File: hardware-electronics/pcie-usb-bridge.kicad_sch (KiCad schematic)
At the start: 0 parts

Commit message: SCH organise schematic #7
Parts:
- added U3: PI7C9X440SLBFDE, M2SmartHomeFootprints:PI7C9X440SLBFDE, symbol M2SmartHomeSymbols:PI7C9X440SLBFDE
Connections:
- new net: U3.100 (VDDC), U3.109 (VDDC), U3.111 (VDDC), U3.22 (VDDC), U3.35 (VDDC), U3.81 (VDDC)
- new net: U3.101 (VSS), U3.106 (VSS), U3.110 (VSS), U3.118 (VSS), U3.120 (VSS), U3.125 (VSS), U3.127 (VSS), U3.129 (VSS), U3.23 (VSS), U3.34 (VSS), U3.36 (VSS), U3.39 (VSS), U3.45 (VSS), U3.50 (VSS), U3.53 (VSS), U3.61 (VSS), U3.68 (VSS), U3.82 (VSS), U3.86 (VSS), U3.89 (VSS), U3.9 (VSS), U3.94 (VSS), U3.96 (VSS)
- new net: U3.105 (VDDR), U3.112 (VDDR), U3.33 (VDDR), U3.67 (VDDR), U3.8 (VDDR)
- new net: U3.115 (VDDA), U3.121 (VDDA), U3.122 (VDDA), U3.128 (VDDA), U3.83 (VDDA), U3.90 (VDDA), U3.91 (VDDA), U3.97 (VDDA)
- new net: U3.40 (AVDD), U3.46 (AVDD), U3.49 (AVDD), U3.60 (AVDD)

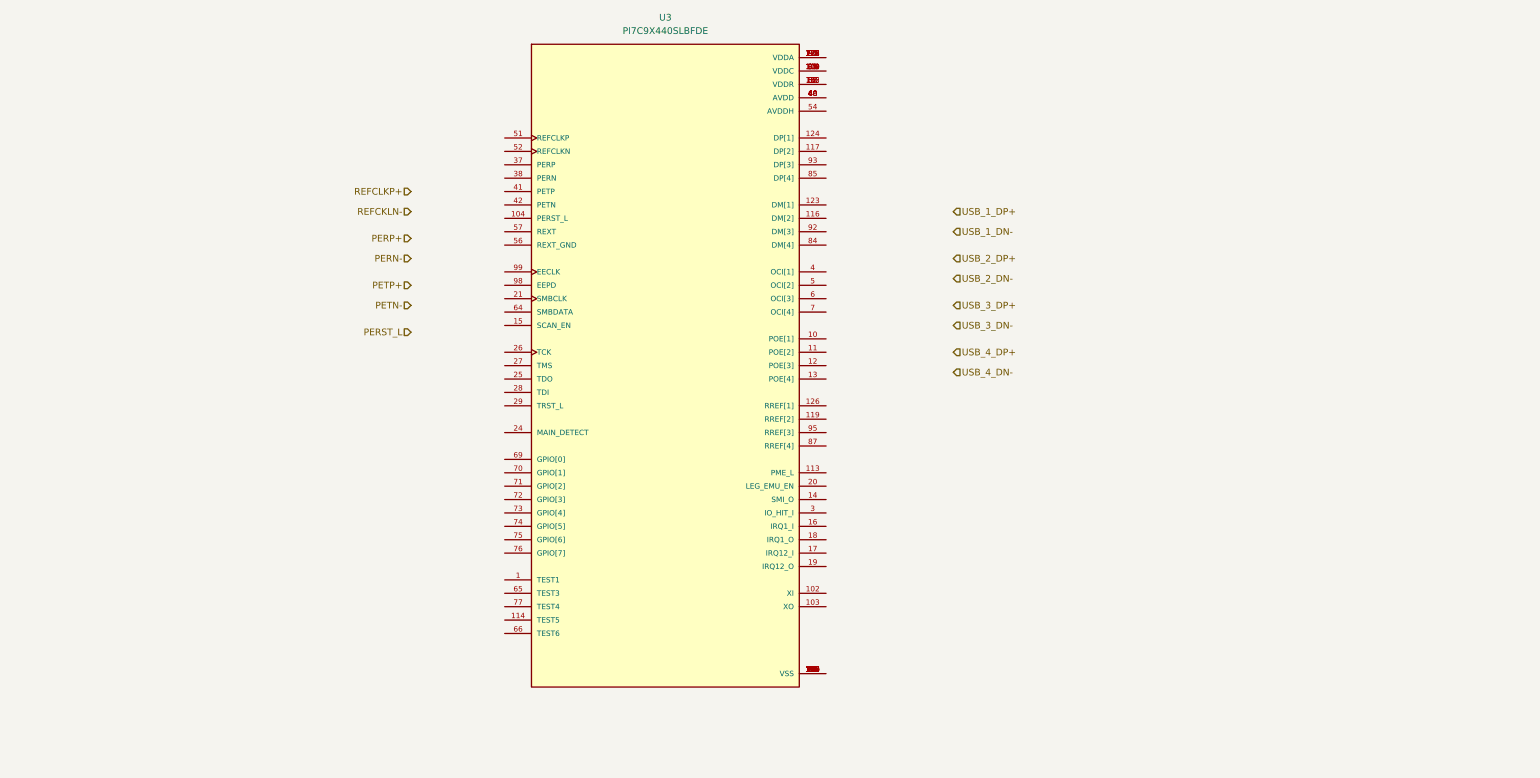
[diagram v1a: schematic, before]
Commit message: WIP SCH EMMC section
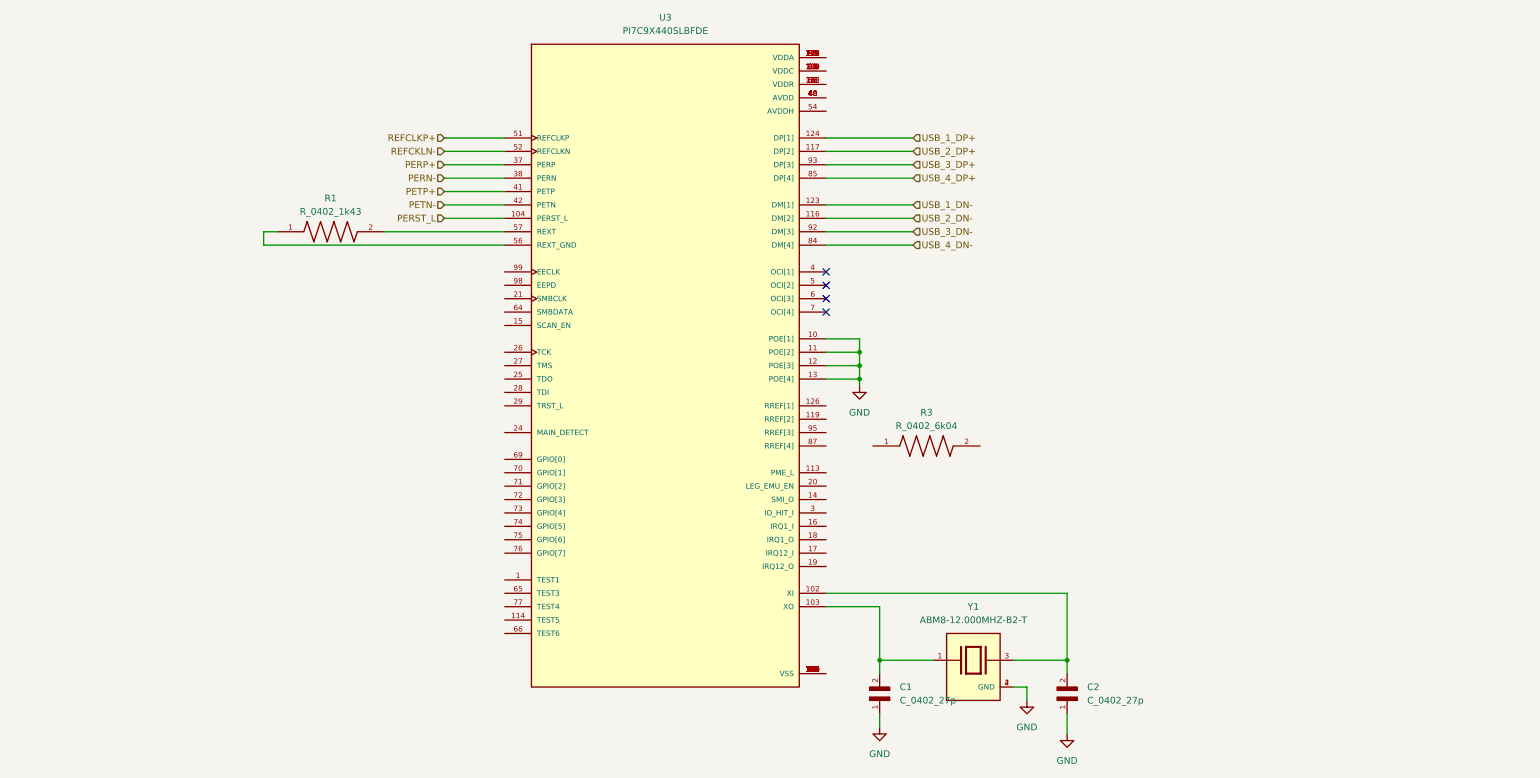
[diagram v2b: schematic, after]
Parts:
- added C1, C2: C_0402_27p, M2SmartHomeFootprints:CAPC1005X56N, symbol M2SmartHomeSymbols:04025A270FAT2A
- added R1: R_0402_1k43, M2SmartHomeFootprints:RESC1005X40N, symbol M2SmartHomeSymbols:RC0402FR-071K43L
- added R3: R_0402_6k04, M2SmartHomeFootprints:RES_ERJ2RKF6041X, symbol M2SmartHomeSymbols:ERJ2RKF6041X
- added Y1: ABM8-12.000MHZ-B2-T, M2SmartHomeFootprints:XTAL_ABM8-12.000MHZ-B2-T, symbol M2SmartHomeSymbols:ABM8-12.000MHZ-B2-T
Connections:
- net PERN-: now also U3.38 (PERN)
- net PERP+: now also U3.37 (PERP)
- net PERST_L: now also U3.104 (PERST_L)
- net PETN-: now also U3.42 (PETN)
- net PETP+: now also U3.41 (PETP)
- net REFCKLN-: now also U3.52 (REFCLKN)
- net REFCLKP+: now also U3.51 (REFCLKP)
- net USB_1_DN-: now also U3.123 (DM[1])
- net USB_1_DP+: now also U3.124 (DP[1])
- net USB_2_DN-: now also U3.116 (DM[2])
- net USB_2_DP+: now also U3.117 (DP[2])
- net USB_3_DN-: now also U3.92 (DM[3])
- net USB_3_DP+: now also U3.93 (DP[3])
- net USB_4_DN-: now also U3.84 (DM[4])
- net USB_4_DP+: now also U3.85 (DP[4])
- net GND: now reaches U3.10 (POE[1])
- net GND: now also U3.11 (POE[2]), U3.12 (POE[3]), U3.13 (POE[4]), C1.1, C2.1, Y1.2 (GND), Y1.4 (GND)
- net at U3.102 (XI): now also C2.2, Y1.3
- net at U3.103 (XO): now also C1.2, Y1.1
- net at U3.56 (REXT_GND): now also R1.1
- net at U3.57 (REXT): now also R1.2
- no-connect marks 0 -> 4

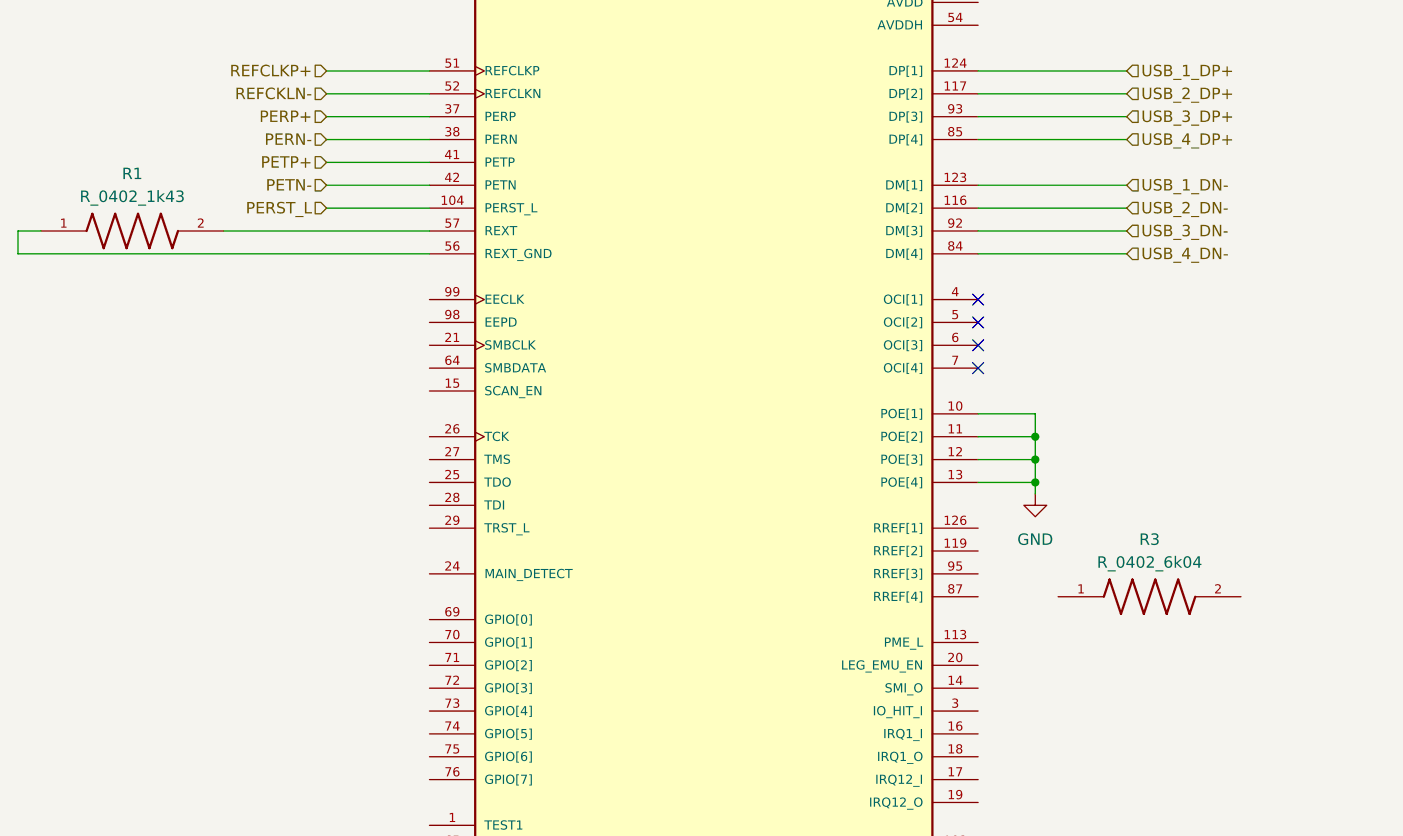
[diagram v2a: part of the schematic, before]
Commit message: [#8] SCH PCIe to USB replaced resistors
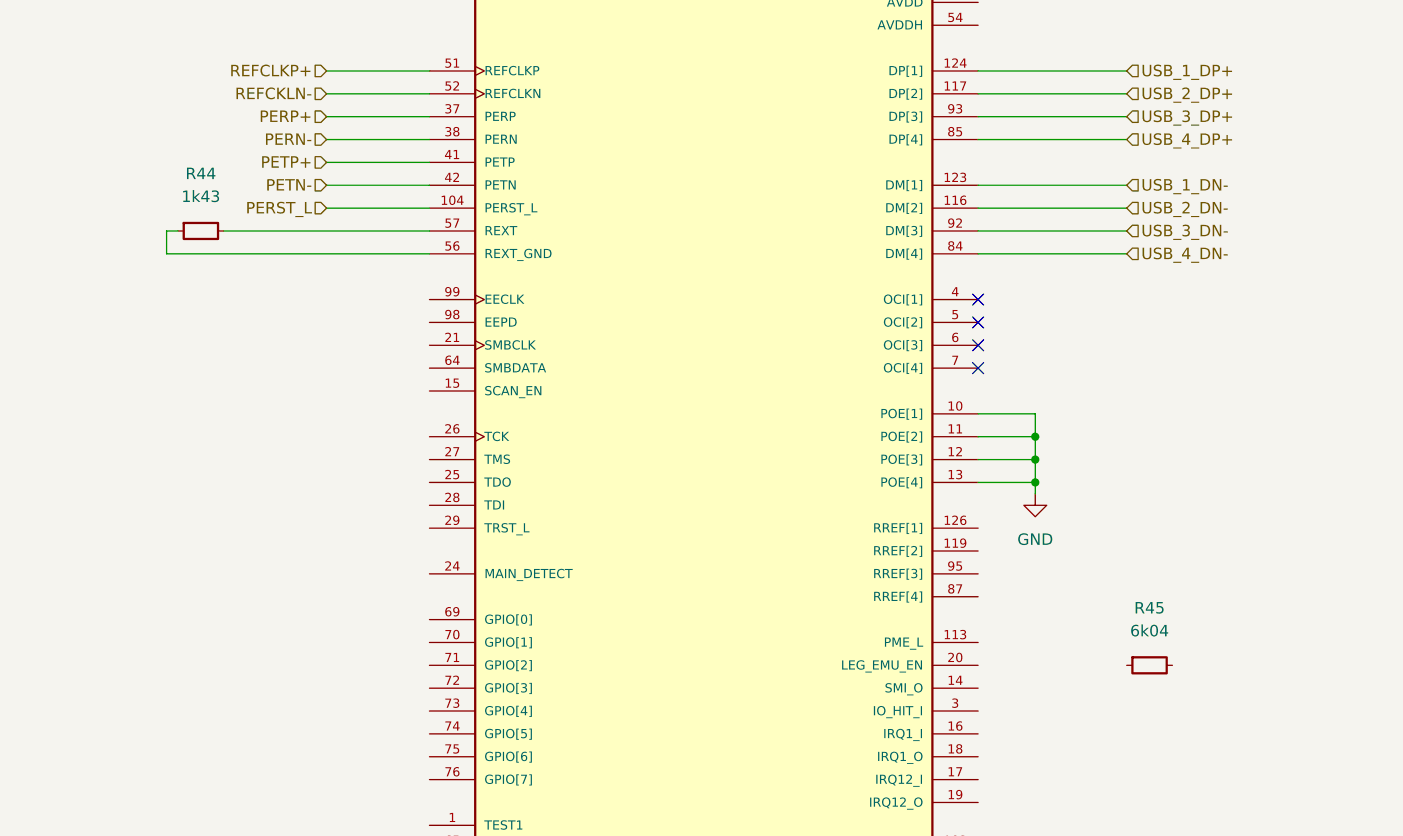
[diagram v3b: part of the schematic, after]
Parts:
- removed R1: R_0402_1k43, M2SmartHomeFootprints:RESC1005X40N, symbol M2SmartHomeSymbols:RC0402FR-071K43L
- removed R3: R_0402_6k04, M2SmartHomeFootprints:RES_ERJ2RKF6041X, symbol M2SmartHomeSymbols:ERJ2RKF6041X
- added R44: R_1k43_0402, M2SmartHomeFootprints:R_0402, symbol M2SmartHomeSymbols:R_1k43_0402
- added R45: R_6k04_0402, M2SmartHomeFootprints:R_0402, symbol M2SmartHomeSymbols:R_6k04_0402
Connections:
- net at U3.56 (REXT_GND): now also R44.1
- net at U3.57 (REXT): now also R44.2

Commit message: [#8] SCH PCIe to USB JTAG connections
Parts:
- added R1, R3: R_5k1_0402, R_5k1_0402:R_0402_1005Metric, symbol M2SmartHomeSymbols:R_5k1_0402
- added TP1, TP2, TP3, TP4, TP5: ~, symbol M2SmartHomeSymbols:TP_SMD_1mm
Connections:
- net GND: now also R1.1, R3.1
- net at U3.25 (TDO): now also TP2.
- net at U3.26 (TCK): now also TP1.
- net at U3.27 (TMS): now also R1.2, TP4.
- net at U3.28 (TDI): now also TP3.
- net at U3.29 (TRST_L): now also R3.2, TP5.

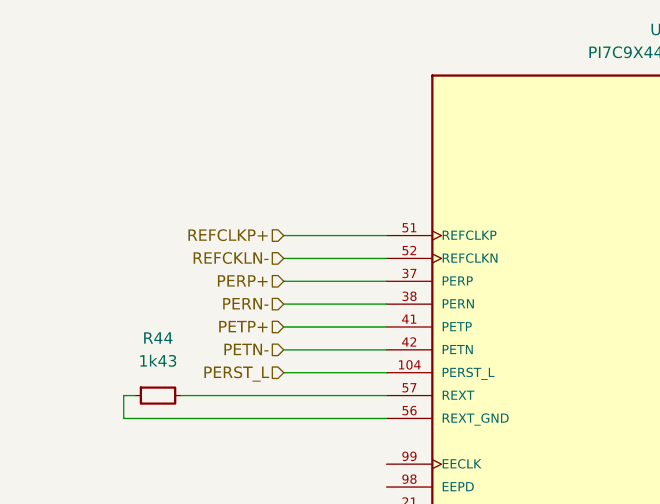
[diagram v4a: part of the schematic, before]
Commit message: [#8] SCH PCIe to USB Add PCIe REFCLK capacitors
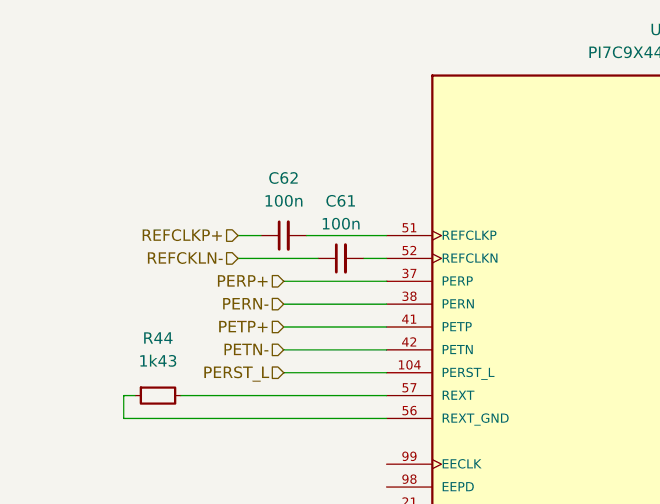
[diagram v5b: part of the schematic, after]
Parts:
- added C61, C62: C_100n_0402, M2SmartHomeFootprints:C_0402, symbol M2SmartHomeSymbols:C_100n_0402
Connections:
- net REFCKLN-: now also C61.1; no longer U3.52 (REFCLKN)
- net REFCLKP+: now also C62.1; no longer U3.51 (REFCLKP)
- new net: C61.2, U3.52 (REFCLKN)
- new net: C62.2, U3.51 (REFCLKP)

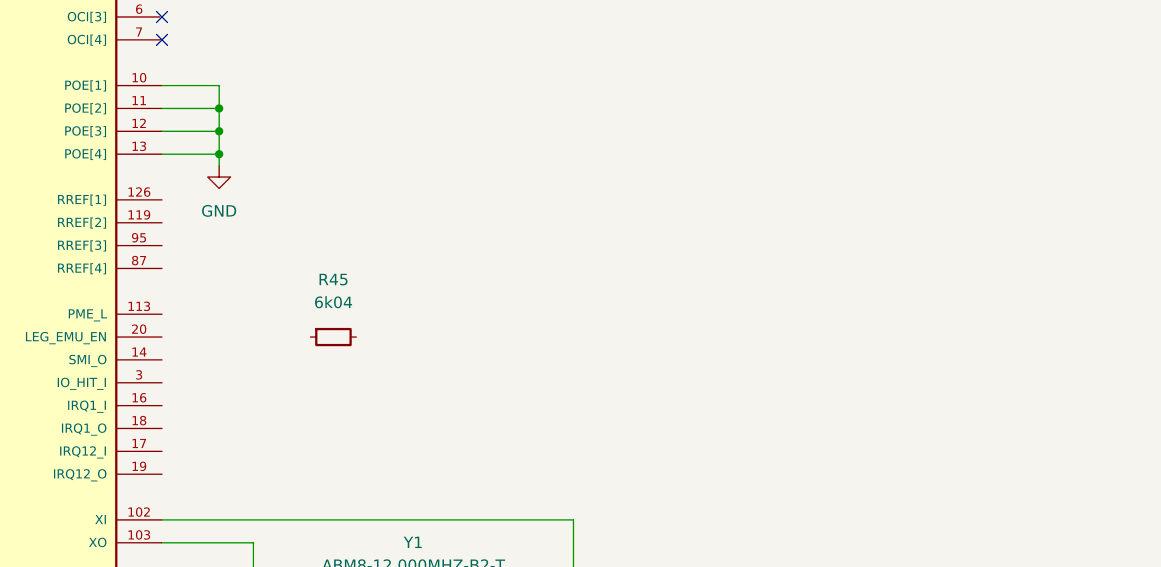
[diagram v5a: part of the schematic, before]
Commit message: [#8] SCH PCIe to USB Add PCIe RREF resistors
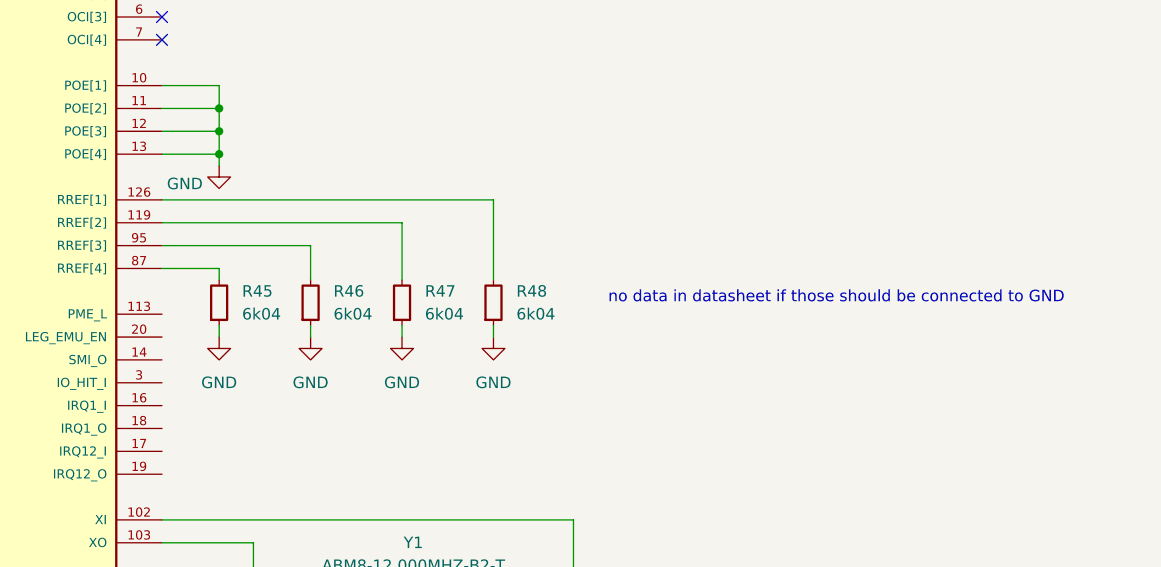
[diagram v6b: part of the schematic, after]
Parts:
- added R46, R47, R48: R_6k04_0402, M2SmartHomeFootprints:R_0402, symbol M2SmartHomeSymbols:R_6k04_0402
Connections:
- net GND: now also R45.1, R46.1, R47.1, R48.1
- net at R45.2: now also U3.87 (RREF[4])
- net at U3.119 (RREF[2]): now also R47.2
- net at U3.126 (RREF[1]): now also R48.2
- net at U3.95 (RREF[3]): now also R46.2
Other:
- note added: "no data in datasheet if those should be connected to GND"
- moved on the sheet: R45
